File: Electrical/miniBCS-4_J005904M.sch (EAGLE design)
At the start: 167 parts, among them IC1 WIZ850io, J14 A0/A1, J2 1734035-2, J3 RCA_DUAL, M2 TEENSY4.1, U1 ADA4084, U10 MAX11300GCM, U11 CAT811, U2 2G17, U3 ISL23425, U4 AD9833, U5 ISO1H815G, U6 78L12, U7 ADM3312/5, U8 2G17, U9 79L12, X1 OSC-OE-CFPS-9, X2 2520-

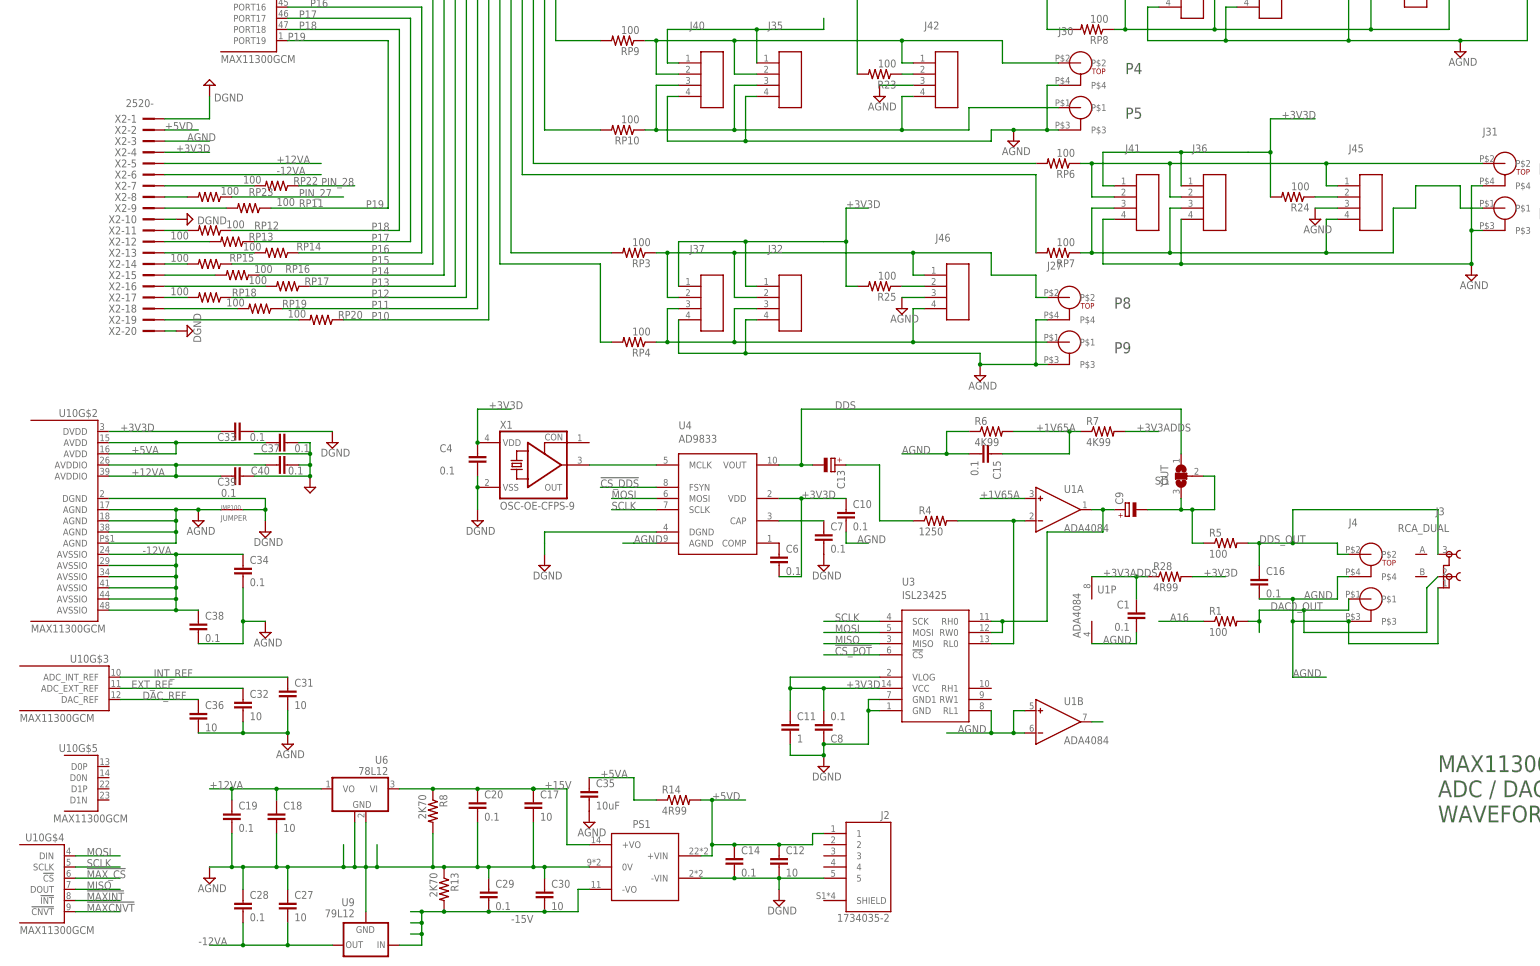
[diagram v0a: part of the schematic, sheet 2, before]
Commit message: Board Update 20240508
Add qwiic and SPI external connections
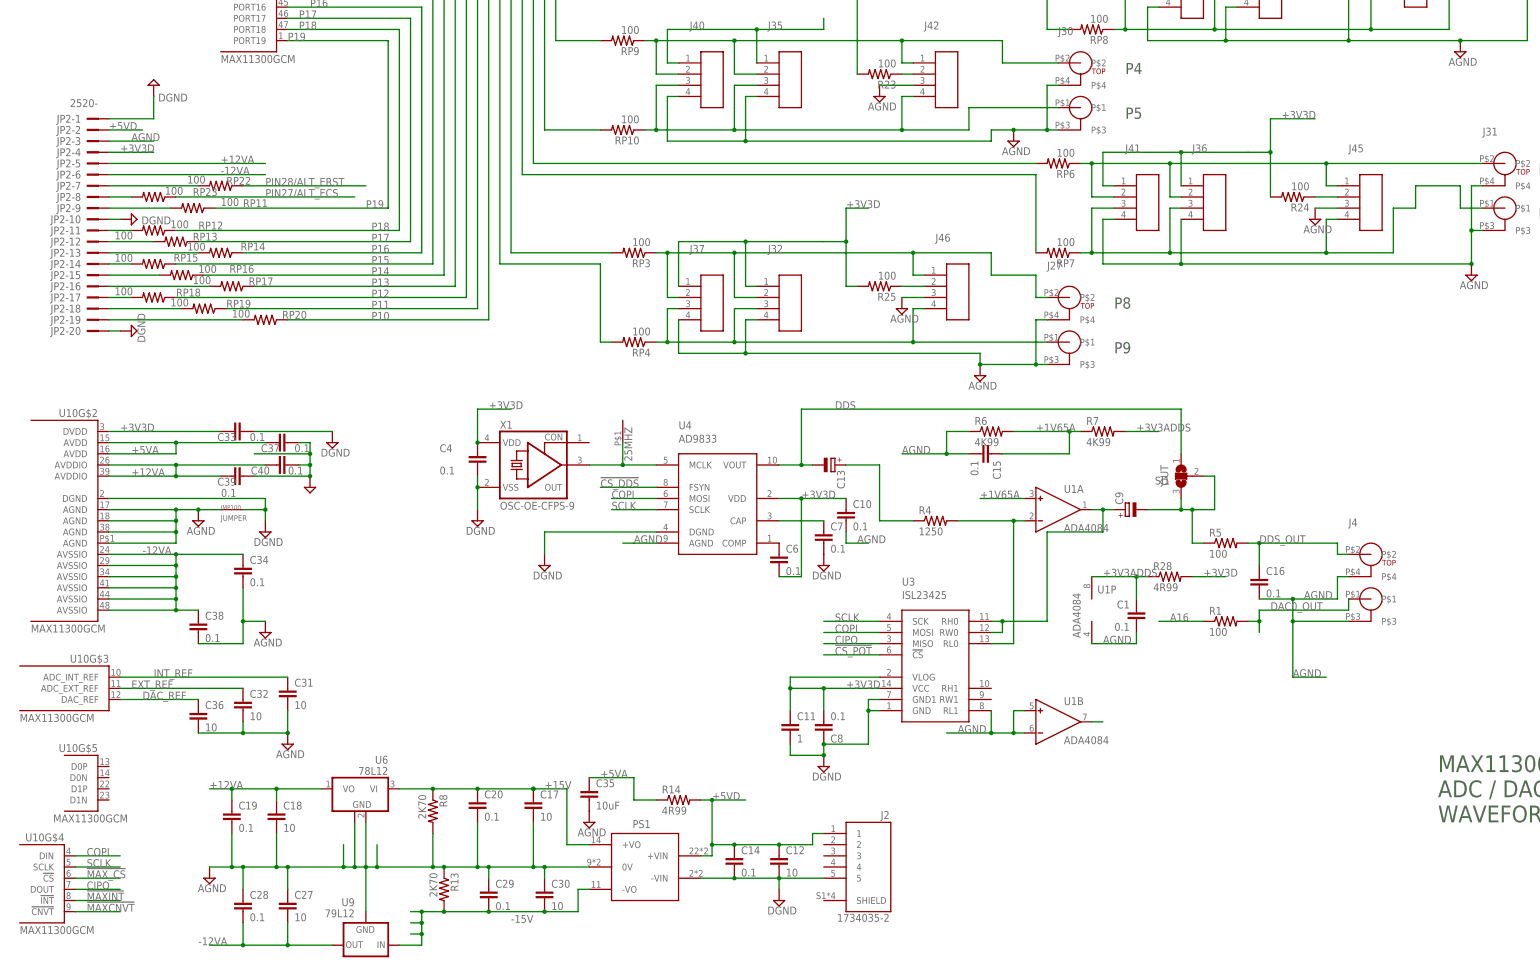
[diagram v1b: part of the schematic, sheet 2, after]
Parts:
- removed SJ10: (no value), jumper:SJ2W
- removed X2: 2520-, con-3m:2520-
- added 25MHZ: (no value), STEVES_BU:CON1
- added ECS: (no value), jumper:SJ2W
- added J11: QWIIC_RIGHT_ANGLE, SparkFun-Connectors:QWIIC_CONNECTORJS-1MM
- added J26: (no value), STEVES_BU:CON2X52X5-3M-THRA
- added JP2: 2520-, con-3m:2520-
- added LOGO1: QWIIC_LOGO_8MM, SparkFun-Aesthetics:QWIIC_LOGO_8MM
- added R2, R3: 4K99, SteveS:RESISTOR_SM0805S
- J3: value RCA_DUAL -> (none); device STEVES_BU:RCA_DUAL -> STEVES_BU:CON7AMPMODU7-RATH
- R26, R27: value 10K0 -> 4K99
- renumbered SJ9 to ERST
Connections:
- net N$52 renamed ERST
- removed net ETH_CS: IC1./SS, M2G$1.25, R27.2, SJ10.2, SJ10.3
- removed net ETH_RST: ERST.2, ERST.3, M2G$1.24, R26.2, U11.!MR
- removed net MISO: IC1.MISO, LCD1.MISO, LCD1.T_MISO, M2G$1.12, U10G$4.DOUT, U3.MISO
- removed net MOSI: IC1.MOSI, LCD1.MOSI, LCD1.T_MOSI, M2G$1.11, U10G$4.DIN, U3.MOSI, U4.MOSI
- removed net PIN_27: M2G$1.27, RP23.1
- removed net PIN_28: M2G$1.28, RP22.1
- new net CIPO: IC1.MISO, J26.6, J3.P$4, LCD1.MISO, LCD1.T_MISO, M2G$1.12, U10G$4.DOUT, U3.MISO
- new net COPI: IC1.MOSI, J26.4, J3.P$3, LCD1.MOSI, LCD1.T_MOSI, M2G$1.11, U10G$4.DIN, U3.MOSI, U4.MOSI
- new net ETH_CS/SDA2: ECS.2, ECS.3, IC1./SS, J11.3, M2G$1.25, R3.2
- new net ETH_RST/SCL2: ERST.2, ERST.3, J11.4, M2G$1.24, R2.2, U11.!MR
- new net PIN27/ALT_ECS: ECS.1, M2G$1.27, R27.2, RP23.1
- new net PIN28/ALT_ERST: ERST.1, M2G$1.28, R26.2, RP22.1
- net +12VA: now also JP2-5.KL; no longer X2-5.KL
- net +3V3D: now also J11.2, J26.9, J3.P$7, JP2-4.KL, R2.1, R3.1; no longer X2-4.KL
- net +5VD: now also JP2-2.KL; no longer X2-2.KL
- net -12VA: now also JP2-6.KL; no longer X2-6.KL
- net AGND: now also JP2-3.KL; no longer J3.1, X2-3.KL
- net DAC0_OUT: no longer J3.2
- net DDS_OUT: no longer J3.3
- net DGND: now also J11.1, J26.1, J26.3, J26.5, J26.7, J3.P$1, JP2-1.KL, JP2-10.KL, JP2-20.KL; no longer X2-1.KL, X2-10.KL, X2-20.KL
- net N$1: now also JP2-8.KL; no longer X2-8.KL
- net N$13: now also 25MHZ.1
- net N$42: now also JP2-14.KL; no longer X2-14.KL
- net N$51: now also JP2-13.KL; no longer X2-13.KL
- net N$53: now also JP2-19.KL; no longer X2-19.KL
- net N$54: now also JP2-18.KL; no longer X2-18.KL
- net N$55: now also JP2-17.KL; no longer X2-17.KL
- net N$56: now also JP2-16.KL; no longer X2-16.KL
- net N$57: now also JP2-15.KL; no longer X2-15.KL
- net N$58: now also JP2-12.KL; no longer X2-12.KL
- net N$59: now also JP2-11.KL; no longer X2-11.KL
- net N$60: now also JP2-9.KL; no longer X2-9.KL
- net N$62: now also JP2-7.KL; no longer X2-7.KL
- net PIN10: now also J26.10, J3.P$6
- net PIN9: now also J26.8, J3.P$5; no longer ERST.1
- net SCLK: now also J26.2, J3.P$2
- net TX2: no longer SJ10.1
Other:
- note added: "CHANGES: **20240507 ** - Add qwiic Connector - change alt ethernet CS and RST from pins 8 and 9 to 27 and 28 - remove DDS RCA jacks - add SPI external connector"
- note added: "SPI EXPANSION"
- note removed: "CHANGES from J - A15/34 mislabelled at CPU, missed connection - same with A6/20"
- note removed: "Expansion"
- moved on the sheet: C41, IC1, R26, R27, RP11, RP12, RP13, RP14, RP15, RP16, RP17, RP18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
